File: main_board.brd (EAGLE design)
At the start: 160 x 100 mm, 59 parts, among them J1 TBL009-254-02GY-2GY, J2 709176001501006, J3 709176001501006, J4 709176001501006, J5 MF-CON-2.54mm-01x02, U1 MAX9019EKA+T, U2 AEM10941-QFN, U3 LTC2956IMS-1#PBF

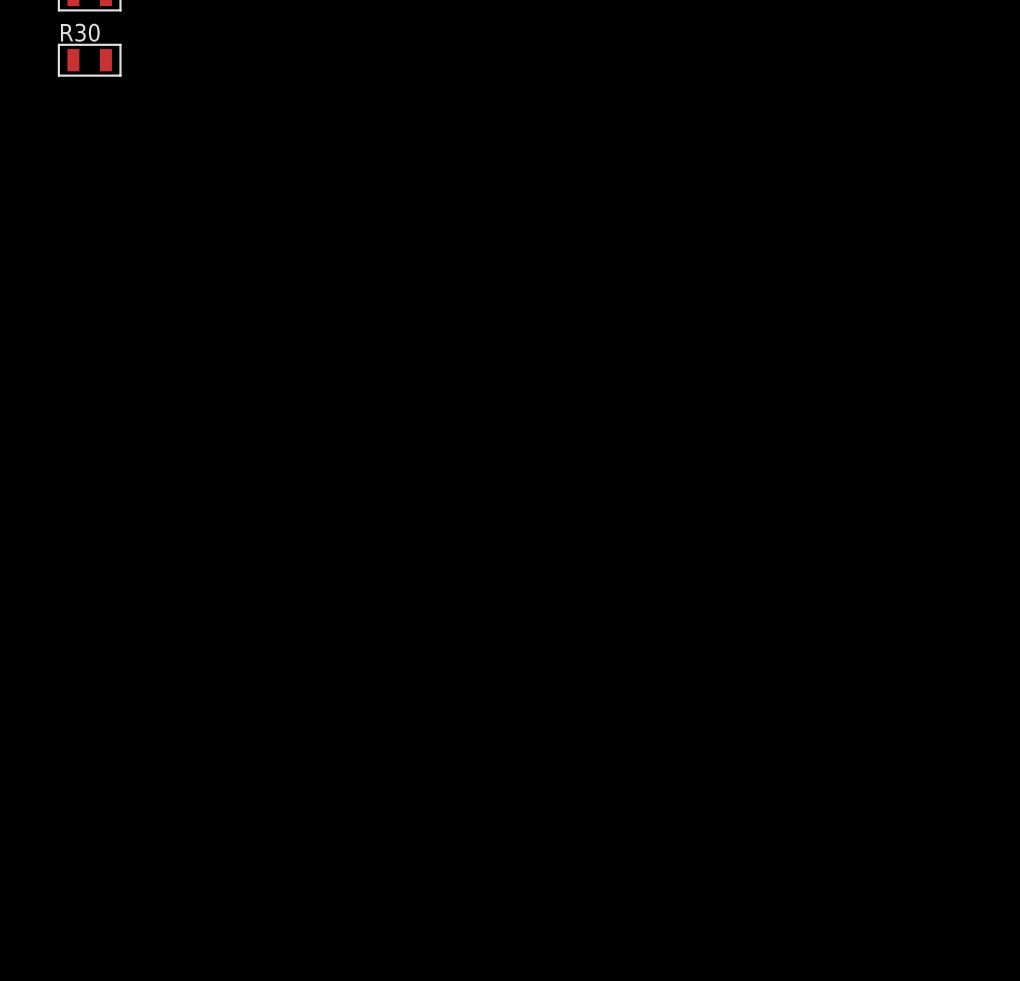
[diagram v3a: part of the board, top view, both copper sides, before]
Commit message: Added analog switch
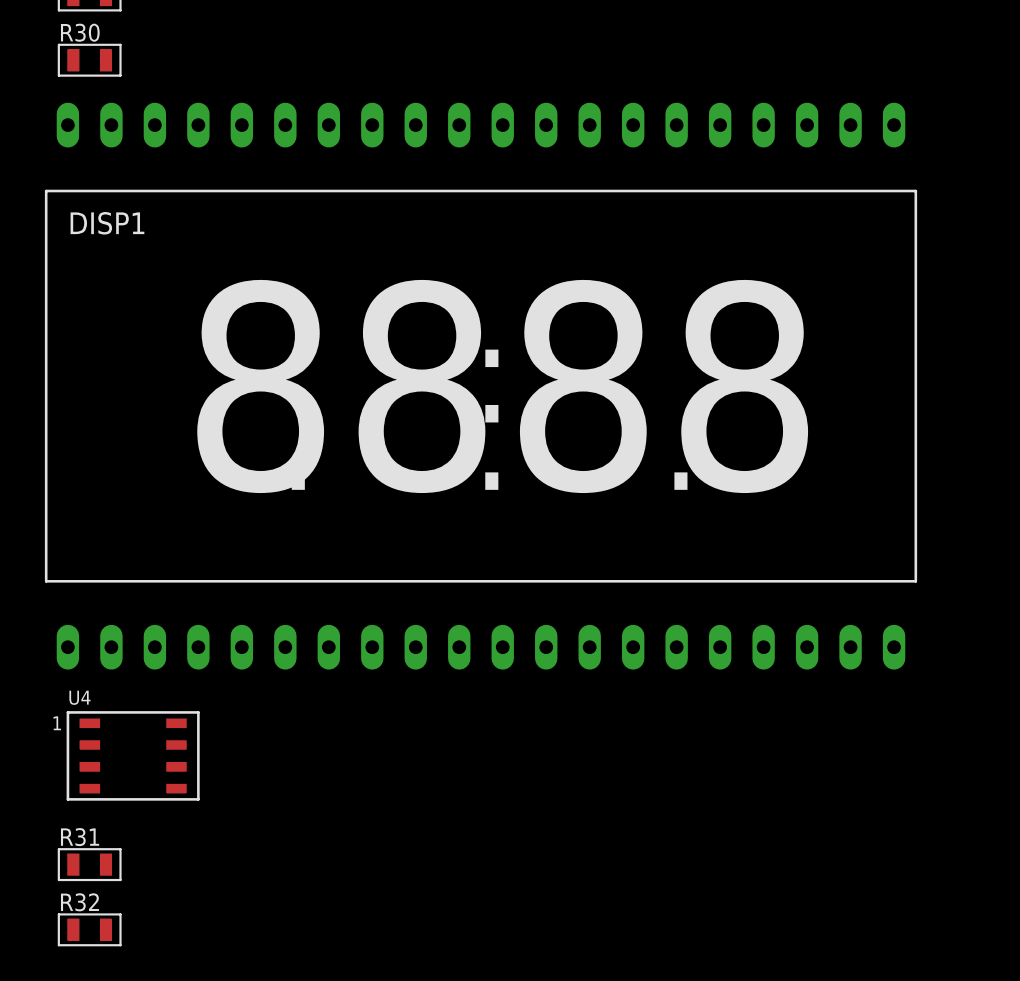
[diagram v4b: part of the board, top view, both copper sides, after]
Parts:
- added DISP1: VI-422-DP-RC-S, PP_Displays:VI-422-DP-RC-S
- added R31: 10K, MF_Passives:R0805
- added R32: 0, MF_Passives:R0805
- added U4: DG469EY-T1-E3, PP_AnalogIC:DG469_SOIC-8
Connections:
- new net !FEED_CAT: DISP1.P$38, U4.P$2
- new net FEED_CAT: DISP1.P$10, DISP1.P$13, DISP1.P$14, DISP1.P$17, DISP1.P$18, DISP1.P$19, DISP1.P$20, DISP1.P$23, DISP1.P$25, DISP1.P$26, DISP1.P$27, DISP1.P$30, DISP1.P$31, DISP1.P$32, DISP1.P$35, DISP1.P$36, DISP1.P$37, DISP1.P$5, DISP1.P$9, U4.P$8
- new net N$4: R32.P$2, U4.P$7
- net !OUT: now also DISP1.P$1, DISP1.P$40
- net 3.3V: now also U4.P$4
- net EN: now also R31.P$1, U4.P$6
- net GND: now also R31.P$2, R32.P$1, U4.P$3
- net OUT: now also U4.P$1
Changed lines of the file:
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@@
 <attribute name="WATTAGE" value="" x="-100.33" y="-176.53" size="1.778" layer="27" display="off"/>
+</element>
+<element name="DISP1" library="PP_Displays" package="VI-422-DP-RC-S" value="VI-422-DP-RC-S" x="-101.6" y="-210.82" smashed="yes">
+<attribute name="MPN" value="VI-422-DP-RC-S" x="-101.6" y="-210.82" size="1.778" layer="27" display="off"/>
+<attribute name="NAME" x="-101.6" y="-185.42" size="1.27" layer="25" font="vector" ratio="16" align="top-left"/>
+</element>
+<element name="U4" library="PP_AnalogIC" package="DG469_SOIC-8" value="DG469EY-T1-E3" x="-97.79" y="-217.17" smashed="yes">
+<attribute name="NAME" x="-101.6" y="-213.36" size="0.8128" layer="25" font="vector" ratio="16" align="top-left"/>
+</element>
+<element name="R31" library="MF_Passives" package="R0805" value="10K" x="-100.33" y="-223.52" smashed="yes">
+<attribute name="HOUSEPART" value="" x="-100.33" y="-223.52" size="1.778" layer="27" display="off"/>
+<attribute name="MPN" value="" x="-100.33" y="-223.52" size="1.778" layer="27" display="off"/>
+<attribute name="NAME" x="-102.13" y="-222.42" size="1.016" layer="25" font="vector" ratio="16"/>
+<attribute name="POPULATE" value="0" x="-100.33" y="-223.52" size="1.778" layer="27" display="off"/>
+<attribute name="TOLERANCE" value="" x="-100.33" y="-223.52" size="1.778" layer="27" display="off"/>
+<attribute name="URL" value="" x="-100.33" y="-223.52" size="1.778" layer="27" display="off"/>
+<attribute name="VOLTAGE" value="" x="-100.33" y="-223.52" size="1.778" layer="27" display="off"/>
+<attribute name="WATTAGE" value="" x="-100.33" y="-223.52" size="1.778" layer="27" display="off"/>
+</element>
+<element name="R32" library="MF_Passives" package="R0805" value="0" x="-100.33" y="-227.33" smashed="yes">
+<attribute name="HOUSEPART" value="" x="-100.33" y="-227.33" size="1.778" layer="27" display="off"/>
+<attribute name="MPN" value="" x="-100.33" y="-227.33" size="1.778" layer="27" display="off"/>
+<attribute name="NAME" x="-102.13" y="-226.23" size="1.016" layer="25" font="vector" ratio="16"/>
+<attribute name="POPULATE" value="0" x="-100.33" y="-227.33" size="1.778" layer="27" display="off"/>
+<attribute name="TOLERANCE" value="" x="-100.33" y="-227.33" size="1.778" layer="27" display="off"/>
+<attribute name="URL" value="" x="-100.33" y="-227.33" size="1.778" layer="27" display="off"/>
+<attribute name="VOLTAGE" value="" x="-100.33" y="-227.33" size="1.778" layer="27" display="off"/>
+<attribute name="WATTAGE" value="" x="-100.33" y="-227.33" size="1.778" layer="27" display="off"/>
 </element>
 </elements>
@@
 <contactref element="R29" pad="P$1"/>
 <contactref element="R30" pad="P$1"/>
+<contactref element="U4" pad="P$3"/>
+<contactref element="R31" pad="P$2"/>
+<contactref element="R32" pad="P$1"/>
 <wire x1="-100.85" y1="-157.48" x2="-101.28" y2="-153.67" width="0" layer="19" extent="1-1"/>
 <wire x1="-100.85" y1="-161.29" x2="-100.85" y2="-157.48" width="0" layer="19" extent="1-1"/>
@@
 <wire x1="-14.29" y1="12.7" x2="-21.495" y2="12.995" width="0" layer="19" extent="1-1"/>
 <wire x1="-14.29" y1="5.08" x2="-14.29" y2="12.7" width="0" layer="19" extent="1-1"/>
+<wire x1="-100.3173" y1="-217.805" x2="-101.28" y2="-176.53" width="0" layer="19" extent="1-1"/>
+<wire x1="-99.38" y1="-223.52" x2="-100.3173" y2="-217.805" width="0" layer="19" extent="1-1"/>
+<wire x1="-101.28" y1="-227.33" x2="-99.38" y2="-223.52" width="0" layer="19" extent="1-1"/>
 </signal>
 <signal name="3.3V">
@@
 <contactref element="C9" pad="P$1"/>
 <contactref element="C11" pad="P$1"/>
+<contactref element="U4" pad="P$4"/>
 <wire x1="-102.35" y1="-157.48" x2="-96.985" y2="-149.665" width="0" layer="19" extent="1-1"/>
 <wire x1="-102.35" y1="-168.91" x2="-102.35" y2="-157.48" width="0" layer="19" extent="1-1"/>
 <wire x1="-94.81" y1="-100.035" x2="-96.985" y2="-149.665" width="0" layer="19" extent="1-1"/>
 <wire x1="-101.6" y1="-92.71" x2="-94.81" y2="-100.035" width="0" layer="19" extent="1-1"/>
+<wire x1="-100.3173" y1="-219.075" x2="-102.35" y2="-168.91" width="0" layer="19" extent="1-1"/>
 <wire x1="-21.27" y1="1.27" x2="-101.6" y2="-92.71" width="0" layer="19" extent="1-1"/>
 <wire x1="-21.27" y1="8.89" x2="-21.27" y2="1.27" width="0" layer="19" extent="1-1"/>
@@
 <contactref element="U1" pad="P$6"/>
 <contactref element="TP5" pad="P$1"/>
+<contactref element="U4" pad="P$1"/>
+<wire x1="-100.3173" y1="-215.265" x2="-100.33" y2="-129.54" width="0" layer="19" extent="1-1"/>
 <wire x1="-14.29" y1="1.27" x2="-100.33" y2="-129.54" width="0" layer="19" extent="1-1"/>
 <wire x1="-19.37" y1="5.08" x2="-14.29" y2="1.27" width="0" layer="19" extent="1-1"/>
@@
 <contactref element="U1" pad="P$7"/>
 <contactref element="TP6" pad="P$1"/>
+<contactref element="DISP1" pad="P$1"/>
+<contactref element="DISP1" pad="P$40"/>
+<wire x1="-101.6" y1="-180.32" x2="-100.33" y2="-135.89" width="0" layer="19" extent="1-1"/>
+<wire x1="-101.6" y1="-210.82" x2="-101.6" y2="-180.32" width="0" layer="19" extent="1-1"/>
 <wire x1="-19.145" y1="14.295" x2="-100.33" y2="-135.89" width="0" layer="19" extent="1-1"/>
 </signal>
@@
 <signal name="EN">
 <contactref element="U3" pad="P$8"/>
+<contactref element="U4" pad="P$6"/>
+<contactref element="R31" pad="P$1"/>
+<wire x1="-95.2627" y1="-217.805" x2="-90.61" y2="-100.035" width="0" layer="19" extent="1-1"/>
+<wire x1="-101.28" y1="-223.52" x2="-95.2627" y2="-217.805" width="0" layer="19" extent="1-1"/>
 </signal>
 <signal name="!PB">
@@
 <wire x1="-99.38" y1="-176.53" x2="-94.81" y2="-99.385" width="0" layer="19" extent="1-1"/>
 </signal>
+<signal name="FEED_CAT">
+<contactref element="DISP1" pad="P$35"/>
+<contactref element="DISP1" pad="P$36"/>
+<contactref element="DISP1" pad="P$37"/>
+<contactref element="DISP1" pad="P$5"/>
+<contactref element="DISP1" pad="P$20"/>
+<contactref element="DISP1" pad="P$23"/>
+<contactref element="DISP1" pad="P$19"/>
+<contactref element="DISP1" pad="P$18"/>
+<contactref element="DISP1" pad="P$17"/>
+<contactref element="DISP1" pad="P$30"/>
+<contactref element="DISP1" pad="P$31"/>
+<contactref element="DISP1" pad="P$32"/>
+<contactref element="DISP1" pad="P$9"/>
+<contactref element="DISP1" pad="P$10"/>
+<contactref element="DISP1" pad="P$25"/>
+<contactref element="DISP1" pad="P$14"/>
+<contactref element="DISP1" pad="P$13"/>
+<contactref element="DISP1" pad="P$26"/>
+<contactref element="DISP1" pad="P$27"/>
+<contactref element="U4" pad="P$8"/>
+<wire x1="-66.04" y1="-180.32" x2="-68.58" y2="-180.32" width="0" layer="19" extent="1-1"/>
+<wire x1="-63.5" y1="-180.32" x2="-66.04" y2="-180.32" width="0" layer="19" extent="1-1"/>
+<wire x1="-58.42" y1="-180.32" x2="-63.5" y2="-180.32" width="0" layer="19" extent="1-1"/>
+<wire x1="-76.2" y1="-180.32" x2="-68.58" y2="-180.32" width="0" layer="19" extent="1-1"/>
+<wire x1="-78.74" y1="-180.32" x2="-76.2" y2="-180.32" width="0" layer="19" extent="1-1"/>
+<wire x1="-81.28" y1="-180.32" x2="-78.74" y2="-180.32" width="0" layer="19" extent="1-1"/>
+<wire x1="-88.9" y1="-180.32" x2="-81.28" y2="-180.32" width="0" layer="19" extent="1-1"/>
+<wire x1="-91.44" y1="-180.32" x2="-88.9" y2="-180.32" width="0" layer="19" extent="1-1"/>
+<wire x1="-93.98" y1="-180.32" x2="-91.44" y2="-180.32" width="0" layer="19" extent="1-1"/>
+<wire x1="-91.44" y1="-210.82" x2="-91.44" y2="-180.32" width="0" layer="19" extent="1-1"/>
+<wire x1="-95.2627" y1="-215.265" x2="-91.44" y2="-210.82" width="0" layer="19" extent="1-1"/>
+<wire x1="-81.28" y1="-210.82" x2="-91.44" y2="-210.82" width="0" layer="19" extent="1-1"/>
+<wire x1="-78.74" y1="-210.82" x2="-81.28" y2="-210.82" width="0" layer="19" extent="1-1"/>
+<wire x1="-71.12" y1="-210.82" x2="-78.74" y2="-210.82" width="0" layer="19" extent="1-1"/>
+<wire x1="-68.58" y1="-210.82" x2="-71.12" y2="-210.82" width="0" layer="19" extent="1-1"/>
+<wire x1="-60.96" y1="-210.82" x2="-68.58" y2="-210.82" width="0" layer="19" extent="1-1"/>
+<wire x1="-58.42" y1="-210.82" x2="-60.96" y2="-210.82" width="0" layer="19" extent="1-1"/>
+<wire x1="-55.88" y1="-210.82" x2="-58.42" y2="-210.82" width="0" layer="19" extent="1-1"/>
+<wire x1="-53.34" y1="-210.82" x2="-55.88" y2="-210.82" width="0" layer="19" extent="1-1"/>
+</signal>
+<signal name="!FEED_CAT">
+<contactref element="DISP1" pad="P$38"/>
+<contactref element="U4" pad="P$2"/>
+<wire x1="-96.52" y1="-180.32" x2="-100.3173" y2="-216.535" width="0" layer="19" extent="1-1"/>
+</signal>
+<signal name="N$4">
+<contactref element="R32" pad="P$2"/>
+<contactref element="U4" pad="P$7"/>
+<wire x1="-95.2627" y1="-216.535" x2="-99.38" y2="-227.33" width="0" layer="19" extent="1-1"/>
+</signal>
 </signals>
